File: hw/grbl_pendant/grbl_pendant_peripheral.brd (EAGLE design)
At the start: 100 x 100 mm, 39 parts, among them IC1 74HC595D

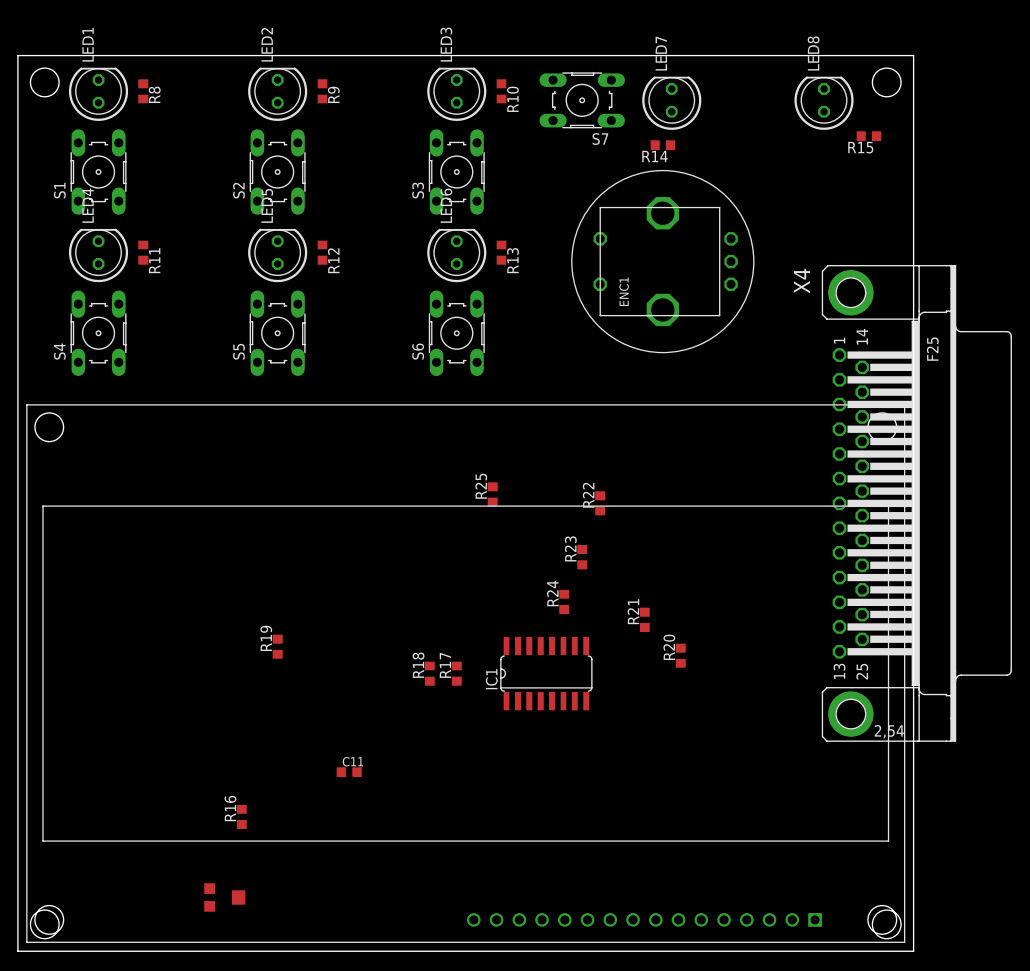
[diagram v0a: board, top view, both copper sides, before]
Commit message: grbl_pendant_peripheral v1 layout
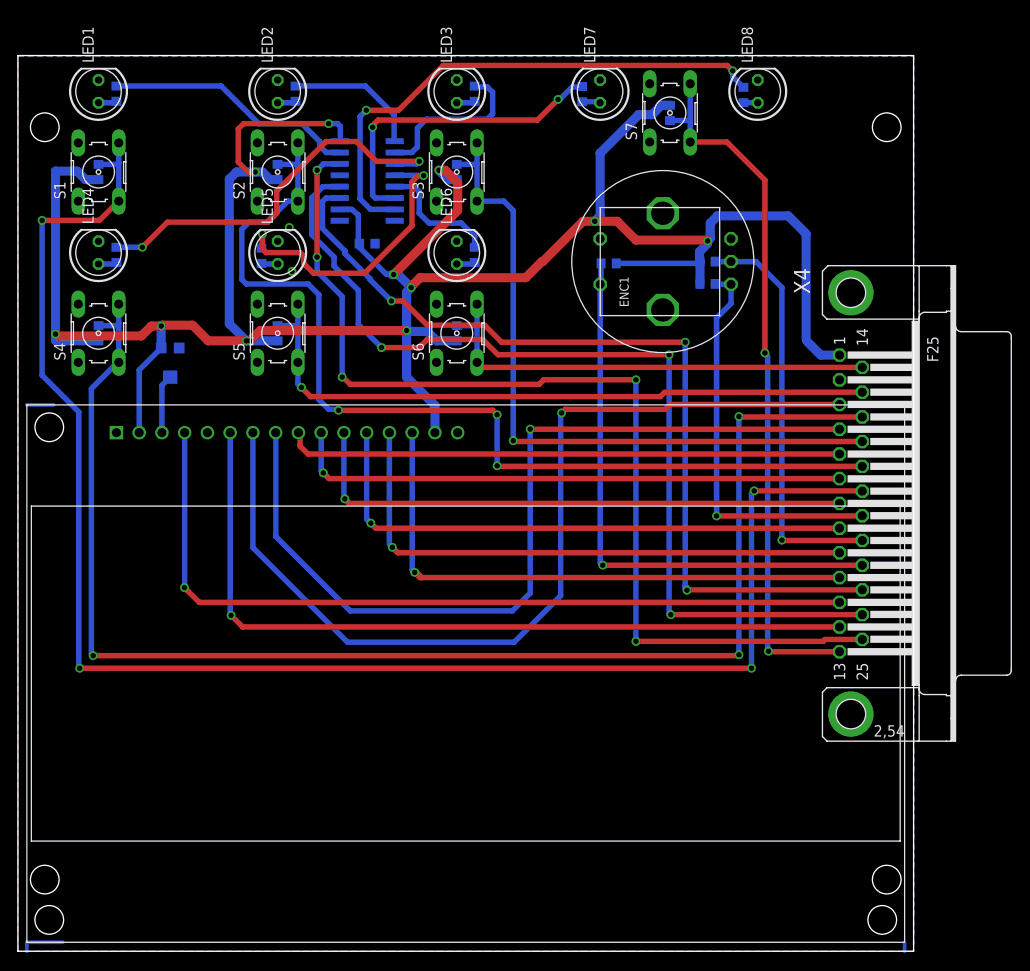
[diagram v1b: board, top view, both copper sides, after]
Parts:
- moved U$1 114.9 mm to (1.00, 1.00), turned to 0 degrees
- moved R16 73.8 mm to (9.00, 87.0), flipped to the bottom
- moved R1 60.1 mm to (17.0, 65.8), flipped to the bottom, turned to 270 degrees
- moved R17 59.5 mm to (29.0, 87.0), flipped to the bottom
- moved C11 59.0 mm to (39.0, 79.0), flipped to the bottom, turned to 180 degrees
- moved IC1 58.5 mm to (39.0, 86.0), flipped to the bottom, turned to 270 degrees
- moved R20 57.6 mm to (29.0, 69.0), flipped to the bottom
- moved R18 56.1 mm to (49.0, 87.0), flipped to the bottom
- moved R25 47.0 mm to (72.8, 93.6), flipped to the bottom, turned to 270 degrees
- moved R24 41.2 mm to (77.0, 77.0), flipped to the bottom, turned to 180 degrees
- moved R19 40.3 mm to (9.00, 69.0), flipped to the bottom
- moved R21 38.3 mm to (49.0, 69.0), flipped to the bottom
- moved R23 33.6 mm to (77.0, 74.5), flipped to the bottom, turned to 180 degrees
- moved R22 26.8 mm to (66.0, 76.8), flipped to the bottom, turned to 0 degrees
- moved R15 14.7 mm to (81.0, 95.6), flipped to the bottom, turned to 270 degrees
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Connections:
- new net LED_SHIFT_SCK: IC1.11, X4.23
- net LED_SHIFT_RCK: now also IC1.12; no longer X4.23
- net LED_SHIFT_SI: now also IC1.14
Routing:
- net +5V: track 0.00 -> 286.6 mm, vias 0 -> 12
- net BTN1: track 0.00 -> 177.0 mm, vias 0 -> 4
- net BTN4: track 0.00 -> 155.6 mm, vias 0 -> 3
- net LED_SHIFT_SI: track 0.00 -> 115.0 mm, vias 0 -> 5
- net BTN2: track 0.00 -> 110.1 mm, vias 0 -> 3
- net LED_SHIFT_RCK: track 0.00 -> 107.5 mm, vias 0 -> 3
- net DISP_D0: track 0.00 -> 105.6 mm, vias 0 -> 1
- net LED_SHIFT_SCK: track 0.00 -> 99.0 mm, vias 0 -> 3
- net DISP_D1: track 0.00 -> 97.1 mm, vias 0 -> 1
- net DISP_RS: track 0.00 -> 91.1 mm, vias 0 -> 1
- net DISP_ENABLE: track 0.00 -> 88.9 mm, vias 0 -> 1
- net BTN_JOG: track 0.00 -> 79.6 mm, vias 0 -> 2
- net BTN3: track 0.00 -> 78.1 mm, vias 0 -> 1
- net BTN5: track 0.00 -> 75.2 mm, vias 0 -> 1
- net DISP_D7: track 0.00 -> 64.4 mm, vias 0 -> 1
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- added copper zone on layer 1, net GND
- added copper zone on layer 16, net GND

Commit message: main board and pendant finished layouts
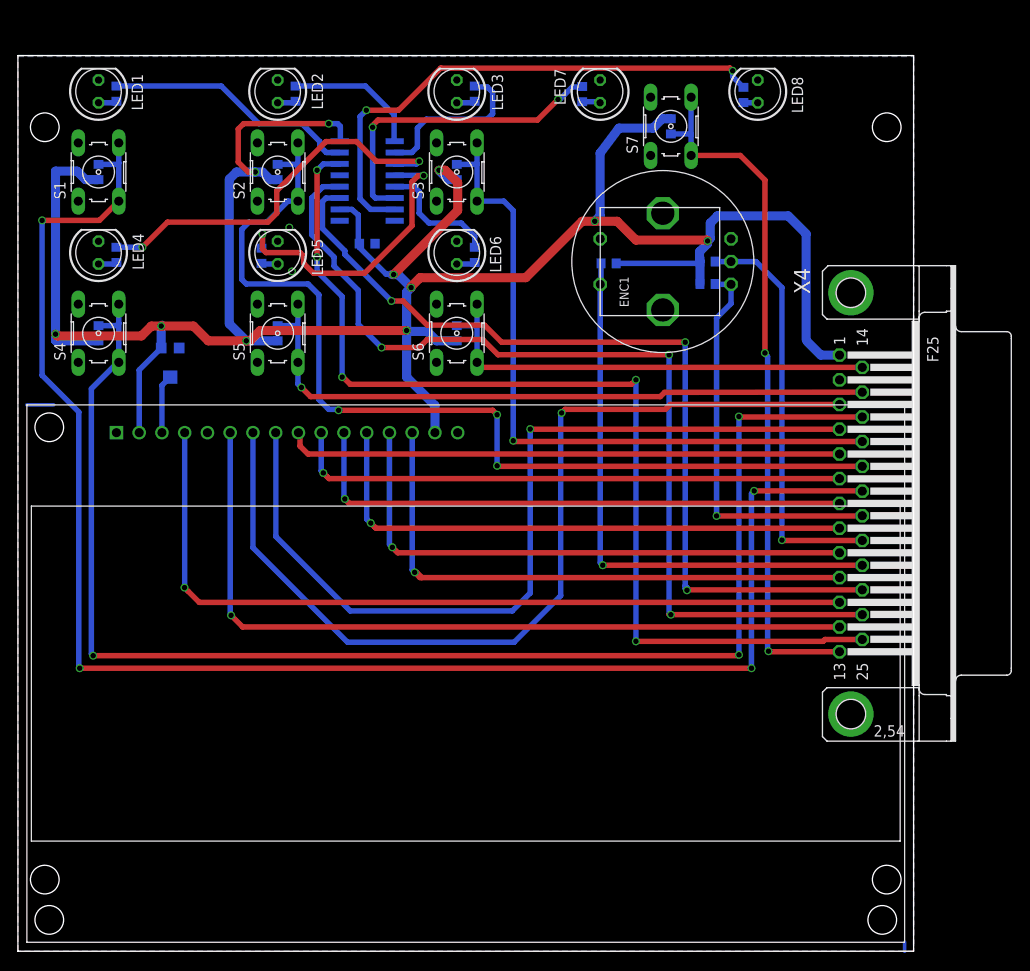
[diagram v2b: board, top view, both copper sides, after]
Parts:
- moved R25 1.50 mm to (72.9, 92.1)
- moved S7 1.50 mm to (72.9, 92.1)
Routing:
- net N$8: track 5.00 -> 0.00 mm
- net BTN_JOG: track 79.6 -> 78.9 mm
- net +5V: track 286.6 -> 286.7 mm, vias 12 -> 11
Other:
- board text added: "Grbl Board Pendant Armin Schlegel 07.09.2015"
